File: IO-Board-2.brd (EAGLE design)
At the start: 160 x 100 mm, 143 parts, among them J1.1 TPPAD1-13, J1.2 TPPAD1-13, J1.3 TPPAD1-13, J1.4 TPPAD1-13, J1.5 TPPAD1-13, J1.6 TPPAD1-13, J1.7 TPPAD1-13, J1.8 TPPAD1-13, J2.1 TPPAD1-13, J2.2 TPPAD1-13, J2.3 TPPAD1-13, J2.4 TPPAD1-13, J2.5 TPPAD1-13, J2.6 TPPAD1-13, J2.7 TPPAD1-13, J2.8 TPPAD1-13, J3.1 TPPAD1-13, J3.2 TPPAD1-13, J3.3 TPPAD1-13, J3.4 TPPAD1-13, J3.5 TPPAD1-13, J3.6 TPPAD1-13, J3.7 TPPAD1-13, J3.8 TPPAD1-13, J4.5 TPPAD1-13, J4.6 TPPAD1-13, J4.7 TPPAD1-13, J4.8 TPPAD1-13

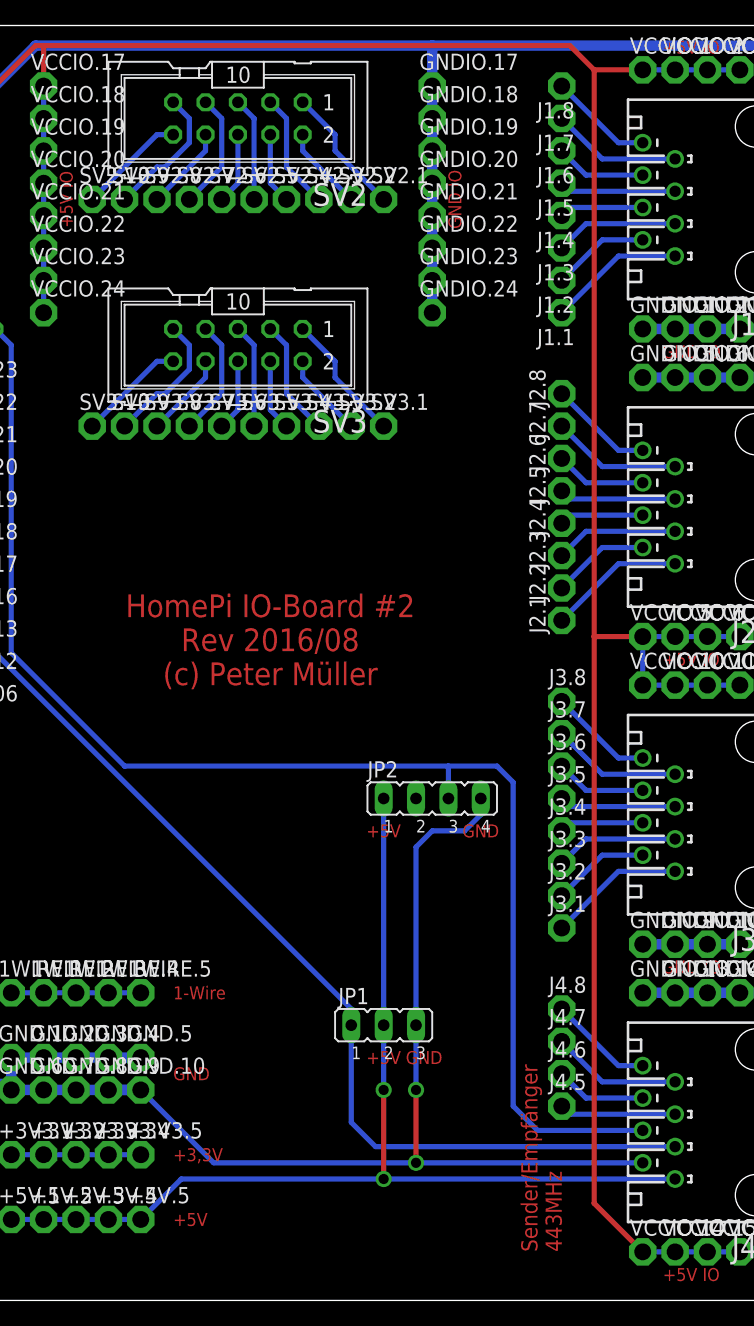
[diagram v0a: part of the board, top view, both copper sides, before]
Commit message: 433MHz-Server und IO-Board-2 Anpassungen
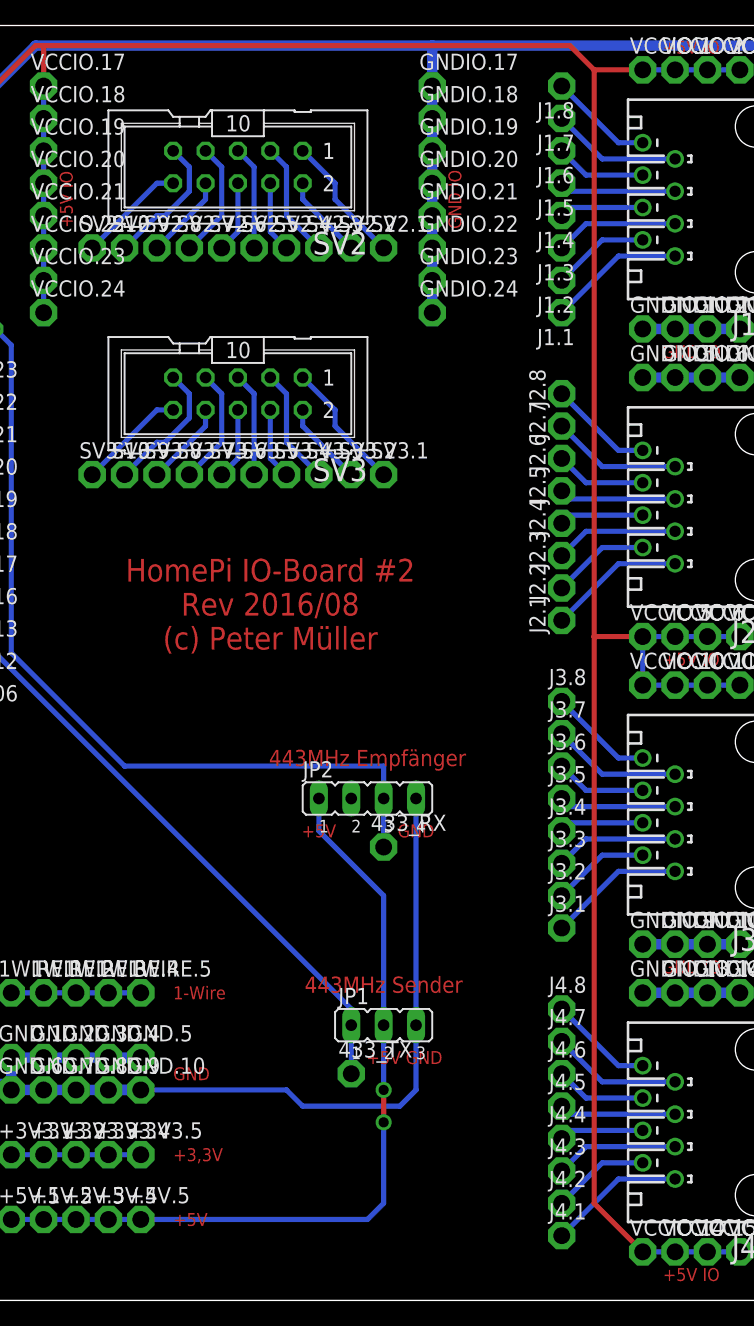
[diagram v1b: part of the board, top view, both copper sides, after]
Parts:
- added 433_RX, 433_TX, J4.1, J4.2, J4.3, J4.4: TPPAD1-13, testpad:P1-13
- moved JP2 5.08 mm to (45.7, 39.4)
- moved SV2.1 3.81 mm to (47.0, 82.5)
- moved SV2.10 3.81 mm to (24.1, 82.5)
- moved SV2.2 3.81 mm to (44.5, 82.5)
- moved SV2.3 3.81 mm to (41.9, 82.5)
- moved SV2.4 3.81 mm to (39.4, 82.5)
- moved SV2.5 3.81 mm to (36.8, 82.5)
- moved SV2.6 3.81 mm to (34.3, 82.5)
- moved SV2.7 3.81 mm to (31.8, 82.5)
- moved SV2.8 3.81 mm to (29.2, 82.5)
- moved SV2.9 3.81 mm to (26.7, 82.5)
- moved SV3 3.81 mm to (35.6, 71.1)
- moved SV3.1 3.81 mm to (47.0, 64.8)
- moved SV3.10 3.81 mm to (24.1, 64.8)
- moved SV3.2 3.81 mm to (44.5, 64.8)
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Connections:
- new net N$1: J4.4, J4.4.TP
- new net N$3: J4.3, J4.3.TP
- new net N$4: J4.2, J4.2.TP
- new net N$5: J4.1, J4.1.TP
- net +5V: no longer J4.1
- net 433MHZ_RX: now also 433_RX.TP; no longer J4.4
- net 433MHZ_TX: now also 433_TX.TP; no longer J4.3
- net GND: no longer J4.2
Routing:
- net 433MHZ_RX: track 108.4 -> 65.2 mm
- net 433MHZ_TX: track 112.2 -> 82.2 mm
- net GND: track 112.3 -> 83.9 mm, vias 2 -> 0
- net +5V: track 98.3 -> 78.7 mm
- net N$5: track 0.00 -> 10.7 mm
- net N$3: track 0.00 -> 9.68 mm
- net N$4: track 0.00 -> 7.67 mm
- net N$1: track 0.00 -> 6.61 mm
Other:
- board text added: "443MHz Empfänger"
- board text added: "443MHz Sender"
- board text removed: "Sender/Empfänger 443MHz"

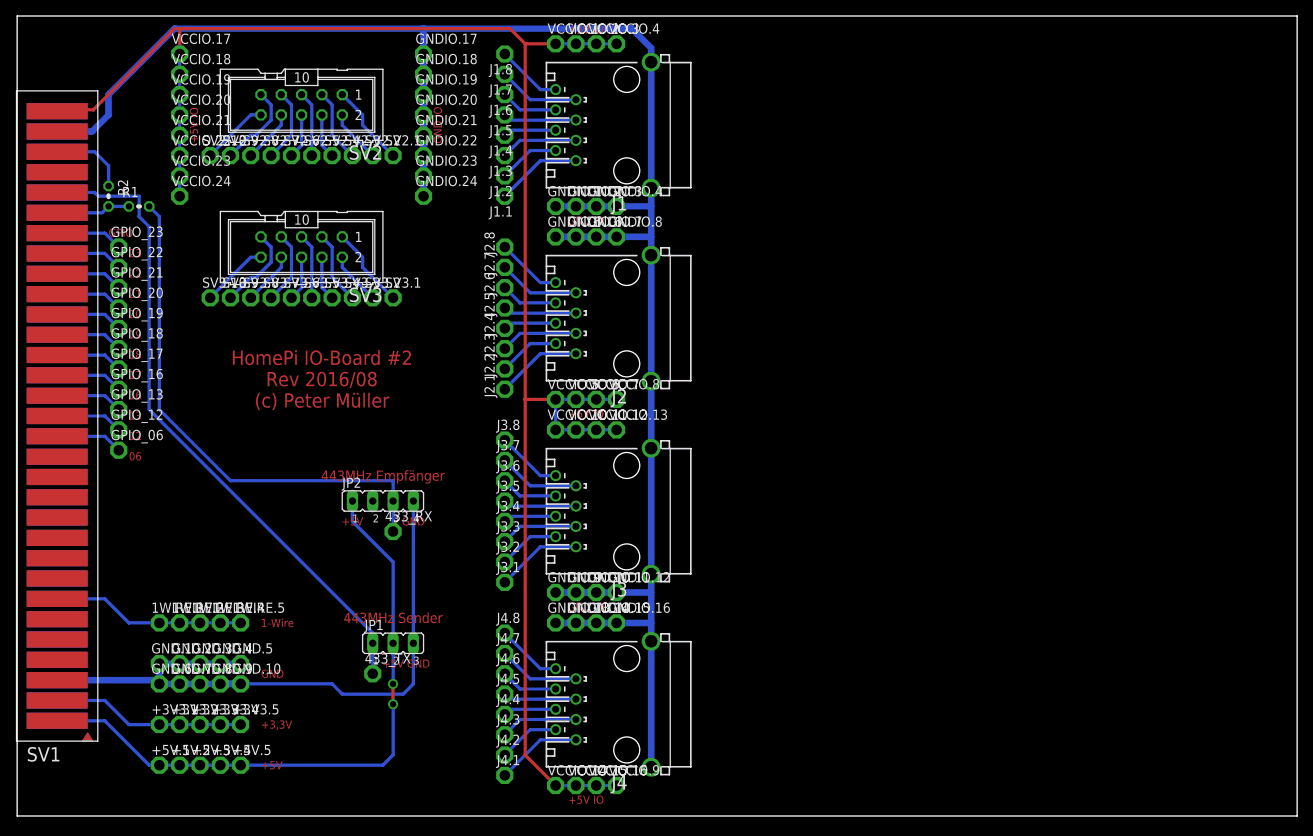
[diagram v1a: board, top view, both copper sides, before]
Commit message: IO-Board und IO-Board-2 Anpassungen
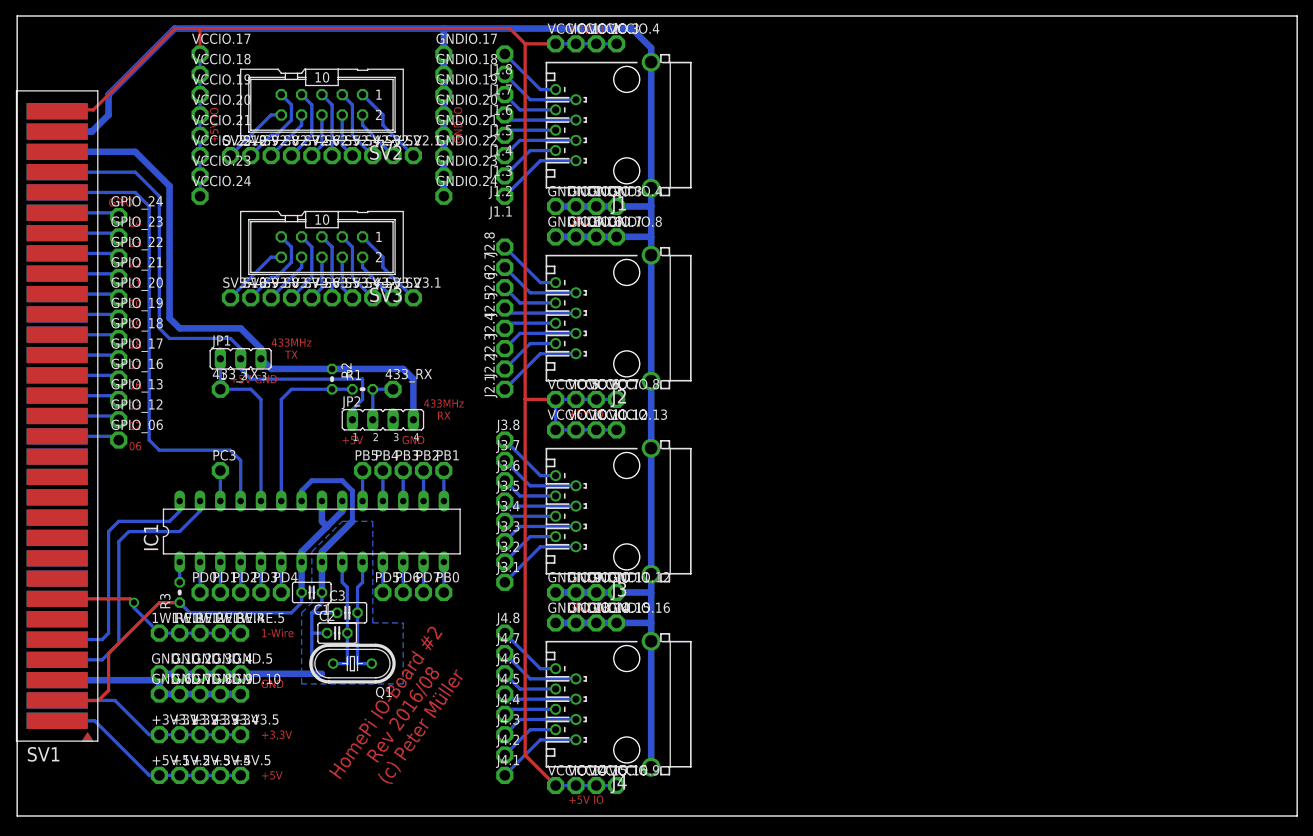
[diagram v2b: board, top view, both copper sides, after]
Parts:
- added C1: 100nF, rcl:C025-025X050
- added C2, C3: 22pF, rcl:C025-025X050
- added GPIO_24, PB0, PB1, PB2, PB3, PB4, PB5, PC3, PD0, PD1, PD2, PD3, PD4, PD5, PD6, PD7: TPPAD1-13, testpad:P1-13
- added IC1: MEGA8-P, atmel:DIL28-3
- added Q1: 8MHz, crystal:HC49U-V
- added R3: 10k, rcl:0204V
- moved 433_TX 40.3 mm to (25.4, 53.3)
- moved JP1 40.3 mm to (27.9, 57.1)
- moved R1 36.1 mm to (43.2, 53.3)
- moved R2 36.1 mm to (39.4, 54.6)
- moved 433_RX 17.8 mm to (47.0, 53.3)
- moved JP2 10.2 mm to (45.7, 49.5)
- moved GNDIO.17 2.54 mm to (53.3, 95.2)
- moved GNDIO.18 2.54 mm to (53.3, 92.7)
- moved GNDIO.19 2.54 mm to (53.3, 90.2)
- moved GNDIO.20 2.54 mm to (53.3, 87.6)
- moved GNDIO.21 2.54 mm to (53.3, 85.1)
- moved GNDIO.22 2.54 mm to (53.3, 82.5)
- moved GNDIO.23 2.54 mm to (53.3, 80.0)
- moved GNDIO.24 2.54 mm to (53.3, 77.5)
- moved SV2.3 2.54 mm to (44.5, 82.5)
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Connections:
- removed net GND.2: R2.1, SV1.29, SV1.29T
- new net +5V_2: JP1.2, JP2.1, SV1.28, SV1.28T
- new net 433MHZ_INT: IC1.25, SV1.27, SV1.27T
- new net GND_2: JP1.3, JP2.4, R2.1, SV1.29, SV1.29T
- new net N$10: IC1.3, PD1.TP
- new net N$11: IC1.4, PD2.TP
- new net N$12: IC1.5, PD3.TP
- new net N$13: IC1.6, PD4.TP
- new net N$14: IC1.11, PD5.TP
- new net N$15: IC1.12, PD6.TP
- new net N$16: IC1.13, PD7.TP
- new net N$17: IC1.14, PB0.TP
- new net N$18: IC1.15, PB1.TP
- new net N$19: IC1.16, PB2.TP
- new net N$20: IC1.17, PB3.TP
- new net N$21: IC1.18, PB4.TP
- new net N$22: IC1.19, PB5.TP
- new net N$23: C3.2, IC1.10, Q1.1
- new net N$24: C2.2, IC1.9, Q1.2
- new net N$6: IC1.1, R3.2
- new net N$7: GPIO_24.TP, SV1.26, SV1.26T
- new net N$8: IC1.26, PC3.TP
- new net N$9: IC1.2, PD0.TP
- net +3V3: now also C1.2, IC1.20, IC1.21, IC1.7, R3.1
- net +5V: no longer JP1.2, JP2.1
- net 433MHZ_RX: now also JP2.2; no longer JP2.3
- net 433MHZ_TX: now also IC1.24; no longer SV1.27, SV1.27T
- net GND: now also C1.1, C2.1, C3.1, IC1.22, IC1.8; no longer JP1.3, JP2.4
- net N$2: now also IC1.23; no longer SV1.26, SV1.26T
- net SCL: now also IC1.28
- net SDA: now also IC1.27
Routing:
- net GND_2: track 0.00 -> 71.8 mm
- net +5V_2: track 0.00 -> 65.7 mm
- net 433MHZ_TX: track 82.2 -> 22.1 mm
- net 433MHZ_INT: track 0.00 -> 59.0 mm
- net 433MHZ_RX: track 65.2 -> 6.35 mm
- net +3V3: track 24.2 -> 82.3 mm
- net +5V: track 78.7 -> 25.8 mm, vias 2 -> 0
- net SDA: track 0.00 -> 34.3 mm
- net SCL: track 0.00 -> 30.7 mm
- net N$24: track 0.00 -> 14.7 mm
- net N$23: track 0.00 -> 14.7 mm
- net N$2: track 9.30 -> 22.1 mm
- net GND.2: track 9.69 -> 0.00 mm
- net N$7: track 0.00 -> 7.89 mm
- net GND: track 83.9 -> 88.1 mm
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- added copper zone on layer 16, net GND
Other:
- board text added: "24"
- board text added: "433MHz RX"
- board text added: "433MHz TX"
- board text removed: "443MHz Empfänger"
- board text removed: "443MHz Sender"

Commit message: IO-Board-2 Anpassung
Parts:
- R1, R2: device rcl:0204V -> rcl:0204/5
- moved JP2 7.73 mm to (53.3, 50.8), turned to 270 degrees
- moved R1 5.39 mm to (47.0, 49.5)
- moved 433_TX 5.08 mm to (25.4, 48.3)
- moved JP1 5.08 mm to (27.9, 52.1)
- moved R2 3.59 mm to (41.9, 52.1)
- moved 433_RX 2.84 mm to (49.5, 52.1), turned to 90 degrees
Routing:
- net GND_2: track 71.8 -> 90.1 mm
- net +5V_2: track 65.7 -> 77.4 mm
- net 433MHZ_TX: track 22.1 -> 16.3 mm
- net N$2: track 22.1 -> 19.4 mm
